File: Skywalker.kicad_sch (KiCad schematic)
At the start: 53 parts

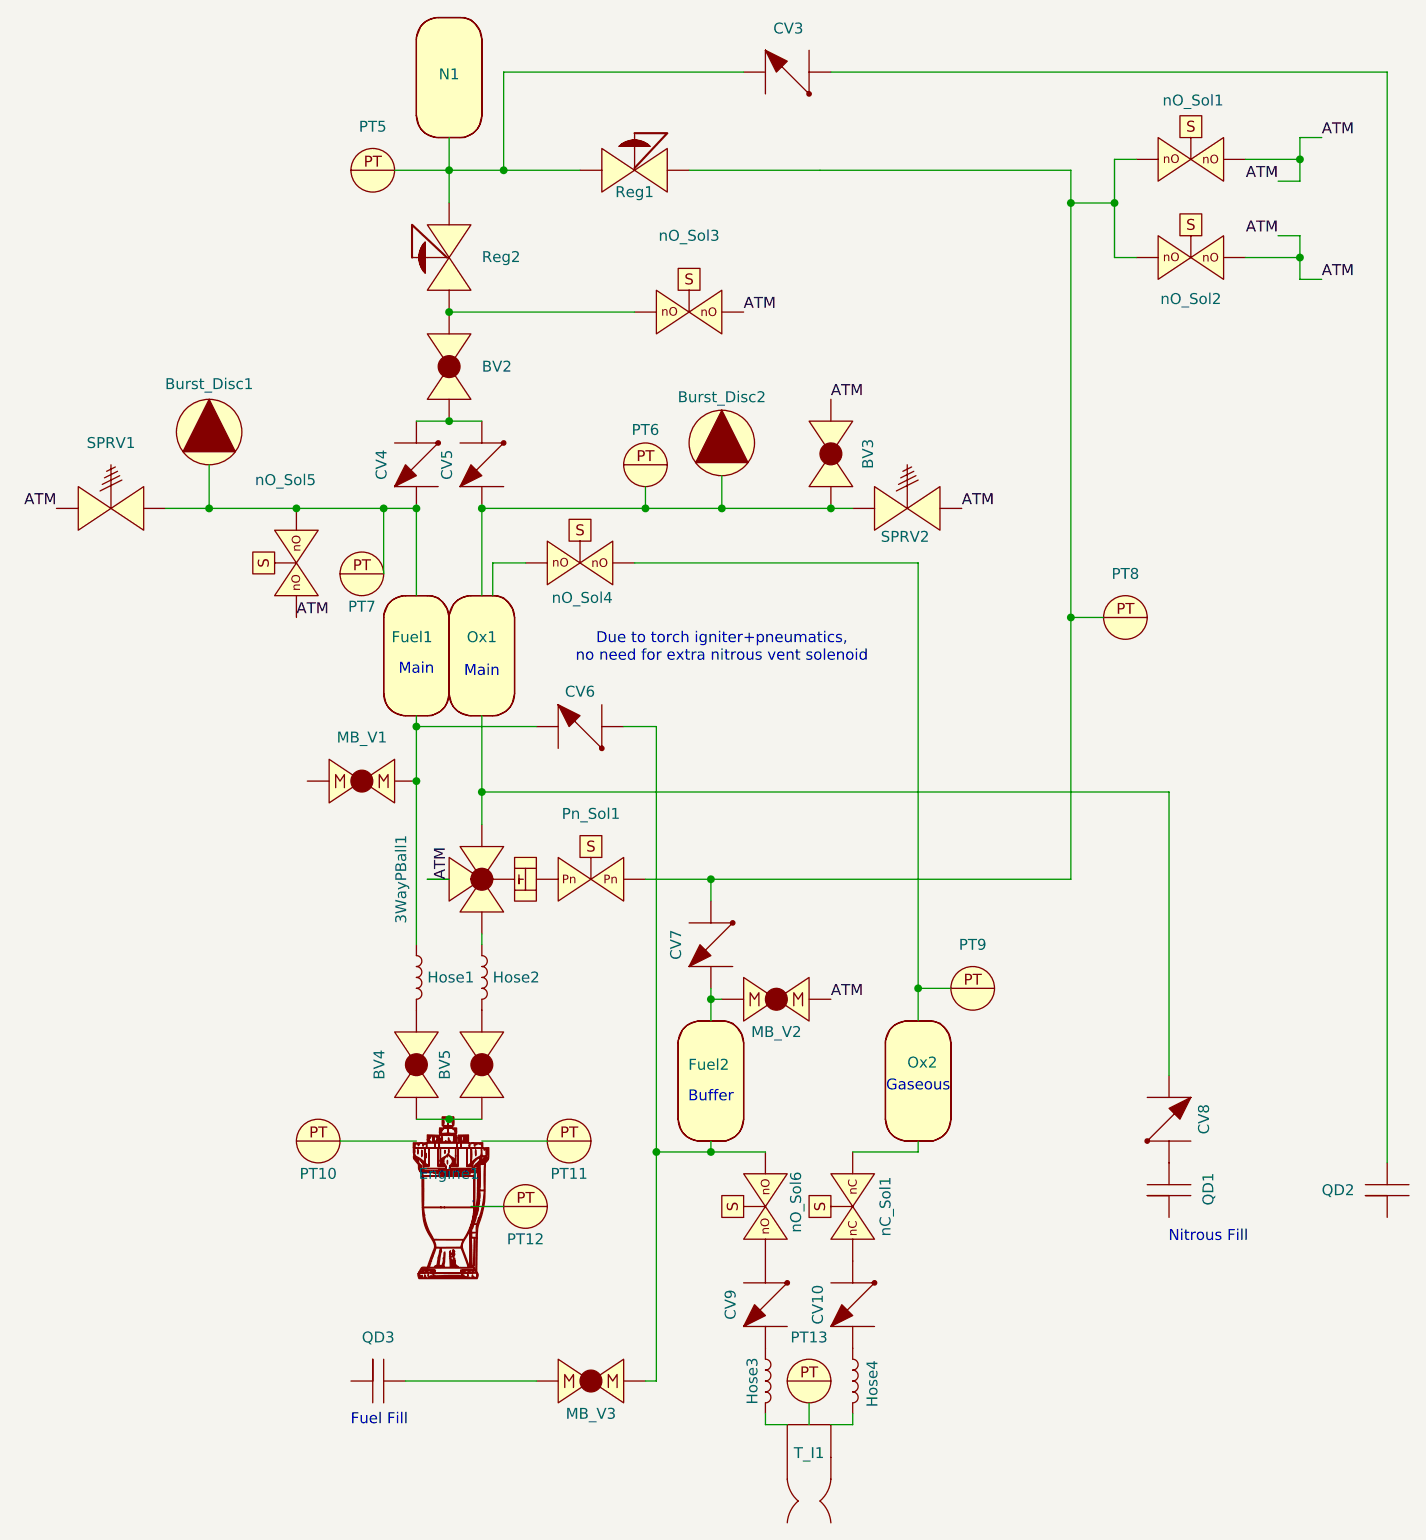
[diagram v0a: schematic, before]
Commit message: Updated igniter PID
+PT +nitrous pressure
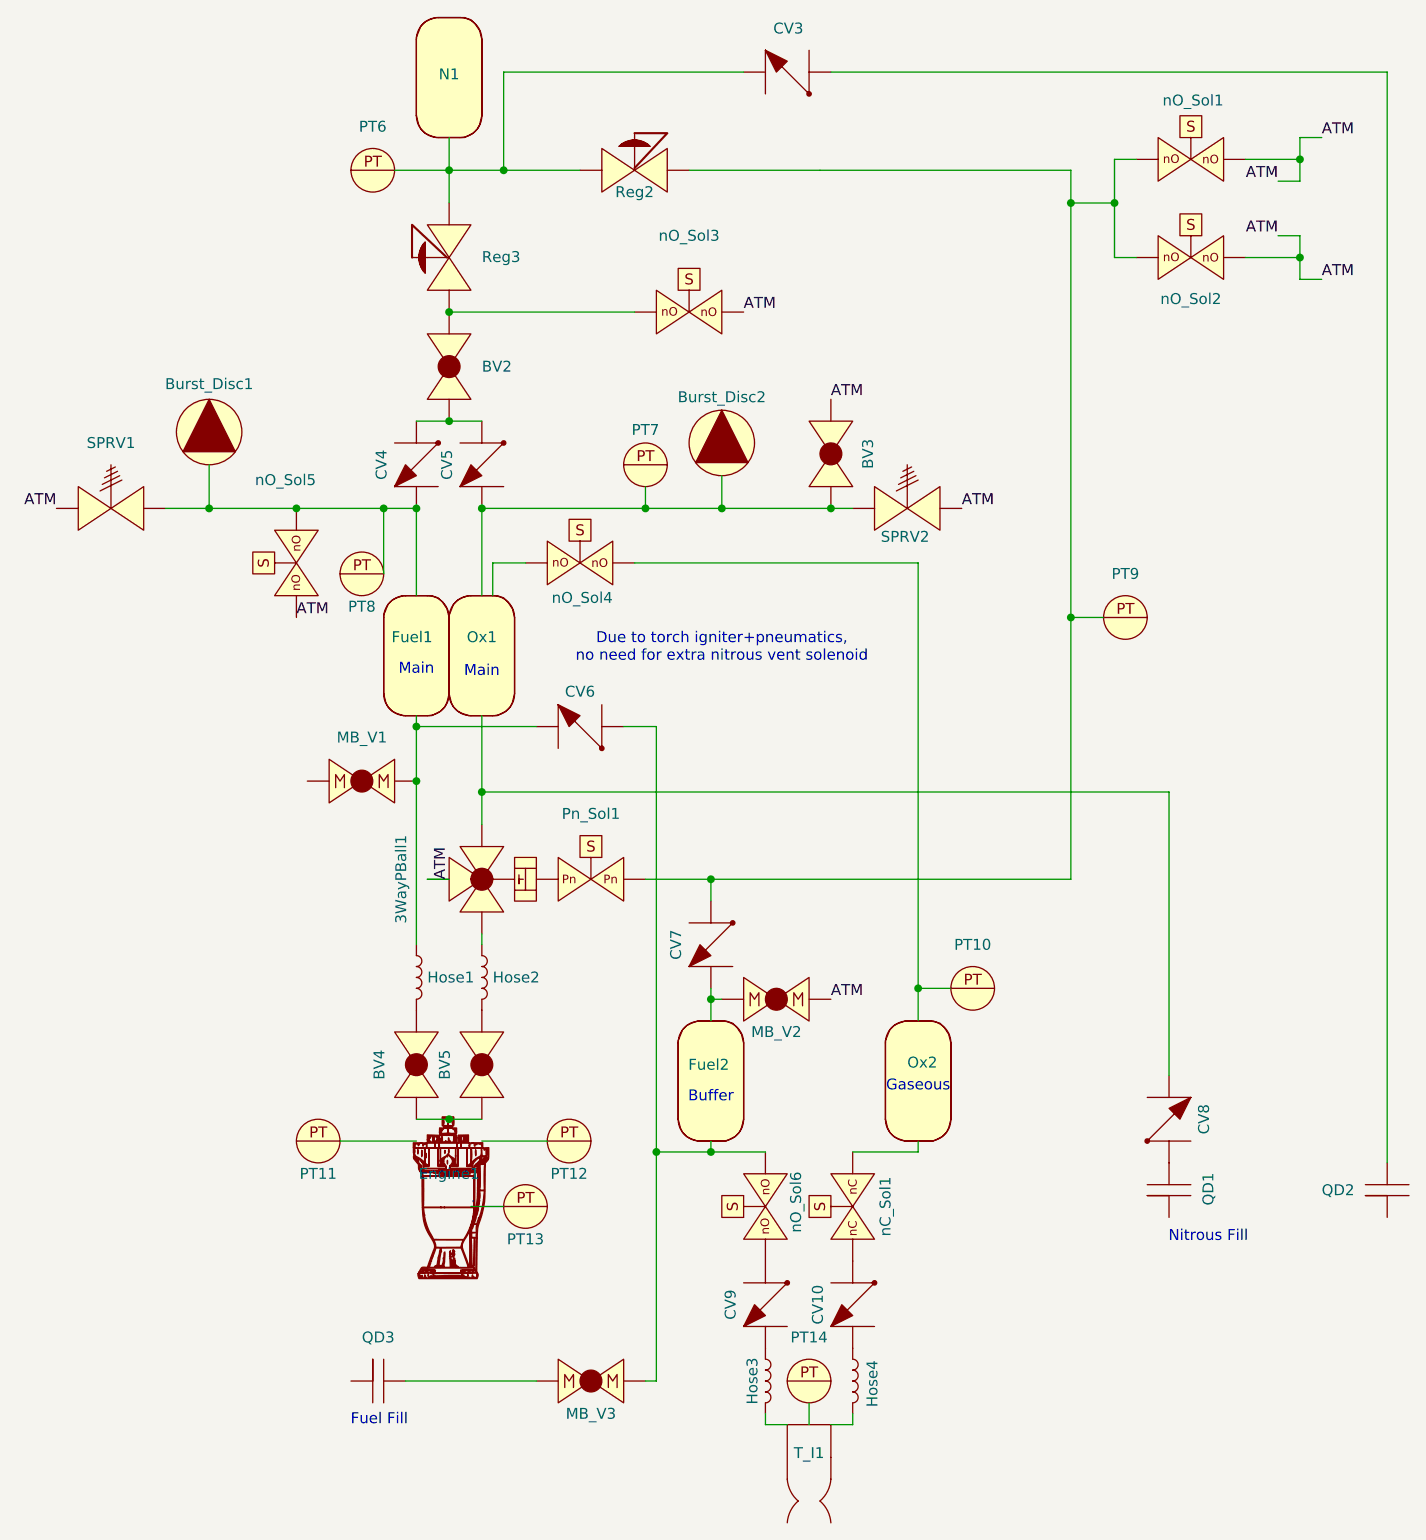
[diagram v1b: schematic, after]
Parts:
- renumbered PT9 to PT10, PT10 to PT11, PT11 to PT12, PT12 to PT13, PT13 to PT14, PT5 to PT6, PT6 to PT7, PT7 to PT8, PT8 to PT9, Reg1 to Reg2, Reg2 to Reg3
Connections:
- net at N1.: now also CV3., PT6., Reg2., Reg3.
- net at Engine1.: now also PT11.; no longer PT12.
- net at PT11.: no longer Engine1.
- net at CV10.: now also Hose4.1; no longer nC_Sol1.
- net at QD1.: now also CV8.
- new net: CV7., PT9., Pn_Sol1., Reg2., nO_Sol1., nO_Sol2.
- new net: CV7., Fuel2., MB_V2.
- new net: Engine1., PT12.
- new net: BV4., BV5., Engine1.
- new net: CV6., Fuel2., MB_V3., nO_Sol6.
- new net: CV10., nC_Sol1.
- new net: Burst_Disc1., CV4., Fuel1., PT8., SPRV1., nO_Sol5.
- new net: BV2., CV4., CV5.
- new net: Ox2., PT10., nO_Sol4.
- new net: 3WayPBall1., CV8., Ox1.
- new net: BV3., Burst_Disc2., CV5., Ox1., PT7., SPRV2.
- now unconnected: Burst_Disc1., Burst_Disc2., PT10., PT6., PT7., PT8., PT9.

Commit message: replaced servo with solenoid
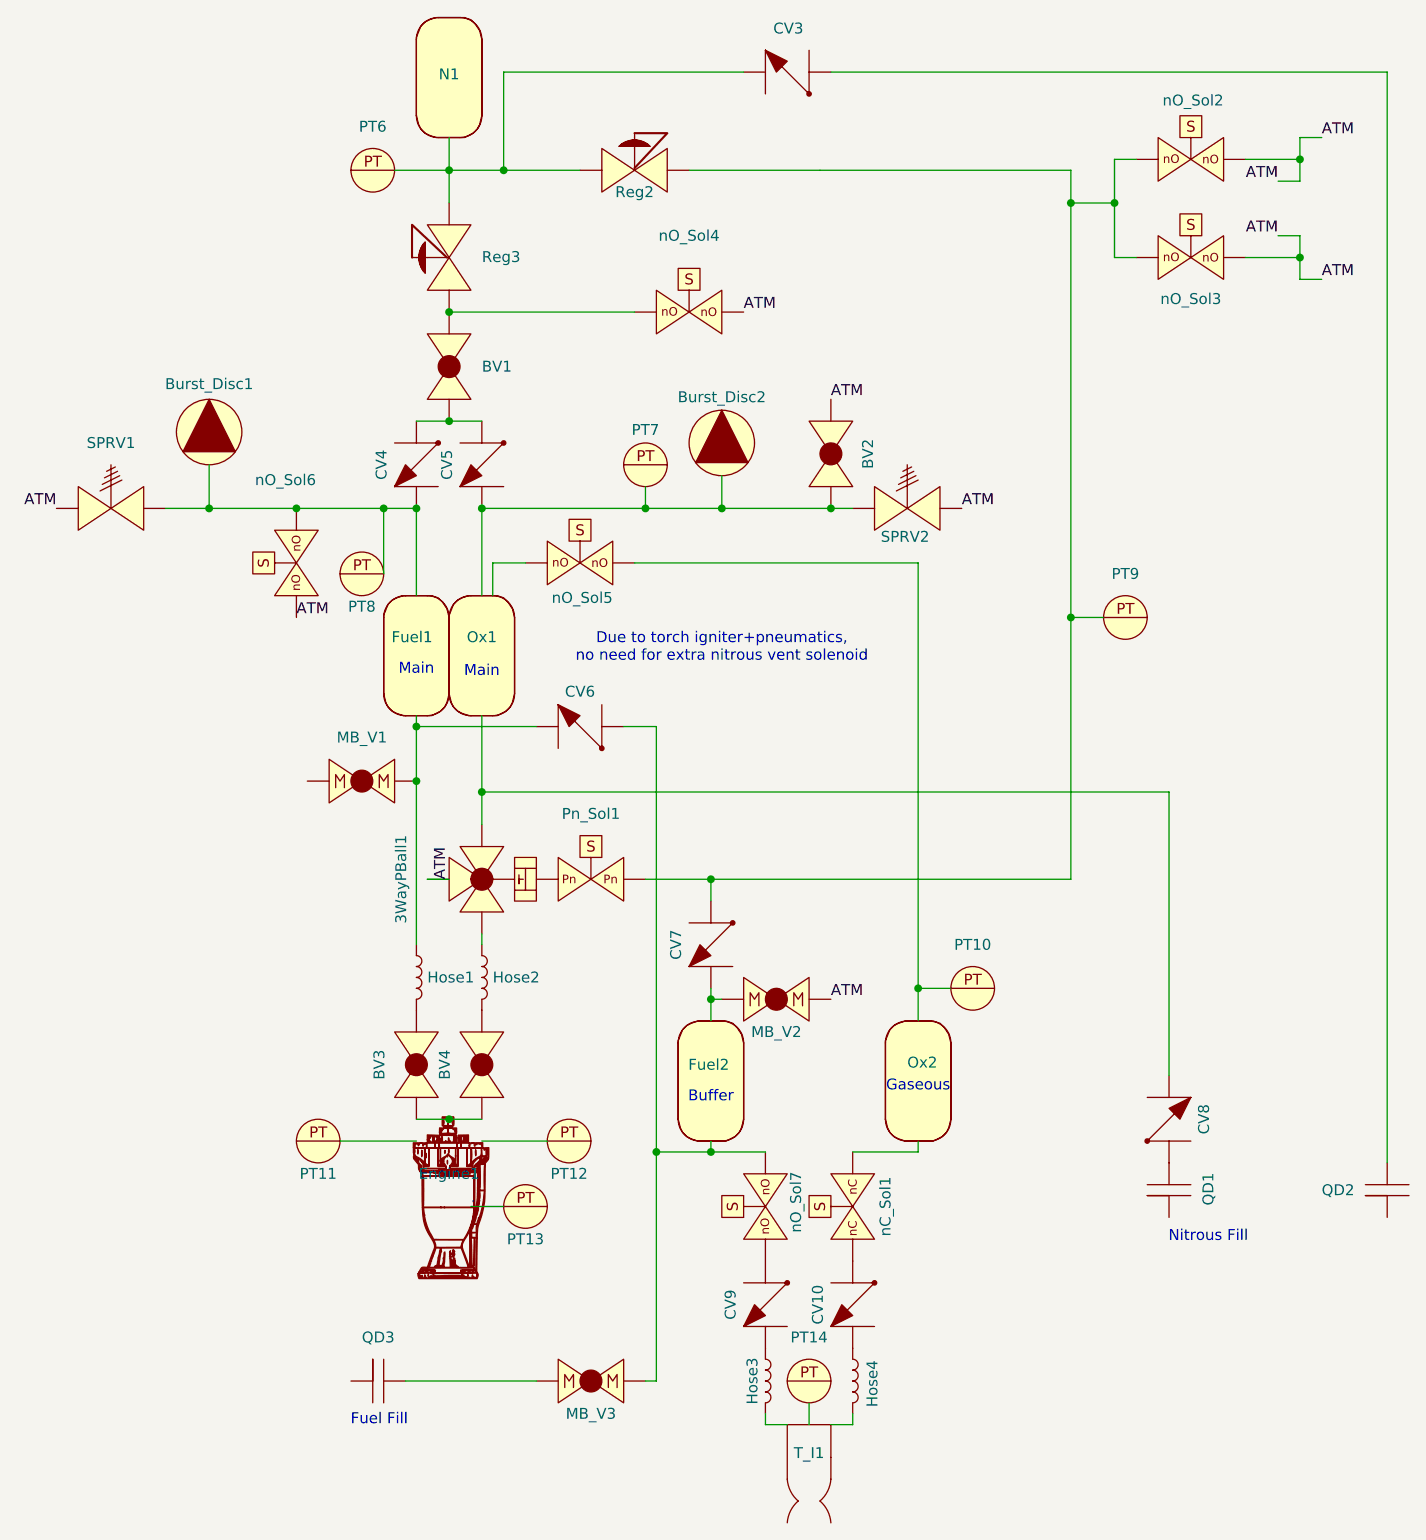
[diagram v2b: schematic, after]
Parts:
- renumbered BV2 to BV1, BV3 to BV2, BV4 to BV3, BV5 to BV4, nO_Sol1 to nO_Sol2, nO_Sol2 to nO_Sol3, nO_Sol3 to nO_Sol4, nO_Sol4 to nO_Sol5, nO_Sol5 to nO_Sol6, nO_Sol6 to nO_Sol7
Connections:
- net at N1.: now also CV3., PT6., Reg2., Reg3.
- net at Engine1.: now also PT11.; no longer PT12.
- net at PT11.: no longer Engine1.
- net at CV10.: now also Hose4.1; no longer nC_Sol1.
- net at QD1.: now also CV8.
- new net: CV7., PT9., Pn_Sol1., Reg2., nO_Sol2., nO_Sol3.
- new net: CV7., Fuel2., MB_V2.
- new net: Engine1., PT12.
- new net: BV3., BV4., Engine1.
- new net: CV6., Fuel2., MB_V3., nO_Sol7.
- new net: CV10., nC_Sol1.
- new net: Burst_Disc1., CV4., Fuel1., PT8., SPRV1., nO_Sol6.
- new net: BV1., CV4., CV5.
- new net: Ox2., PT10., nO_Sol5.
- new net: 3WayPBall1., CV8., Ox1.
- new net: BV2., Burst_Disc2., CV5., Ox1., PT7., SPRV2.
- now unconnected: Burst_Disc1., Burst_Disc2., PT10., PT6., PT7., PT8., PT9.
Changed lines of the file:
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@@
 		(on_board yes)
 		(dnp no)
-		(property "Reference" "BV5"
+		(property "Reference" "BV4"
 			(at 62.992 138.43 0)
 			(effects
@@
 			(project "P_IDs"
 				(path "/045f1f05-3134-4b6d-91b6-463031104f1e/8ff5724e-b29b-49c2-a1fa-190081404476"
-					(reference "BV5")
+					(reference "BV4")
 					(unit 1)
 				)
@@
 		(on_board yes)
 		(dnp no)
-		(property "Reference" "nO_Sol1"
+		(property "Reference" "nO_Sol2"
 			(at 150.114 26.162 0)
 			(effects
@@
 			(project "P_IDs"
 				(path "/045f1f05-3134-4b6d-91b6-463031104f1e/8ff5724e-b29b-49c2-a1fa-190081404476"
-					(reference "nO_Sol1")
+					(reference "nO_Sol2")
 					(unit 1)
 				)
@@
 		(on_board yes)
 		(dnp no)
-		(property "Reference" "BV3"
+		(property "Reference" "BV2"
 			(at 112.268 67.31 0)
 			(effects
@@
 			(project "P_IDs"
 				(path "/045f1f05-3134-4b6d-91b6-463031104f1e/8ff5724e-b29b-49c2-a1fa-190081404476"
-					(reference "BV3")
+					(reference "BV2")
 					(unit 1)
 				)
@@
 		(on_board yes)
 		(dnp no)
-		(property "Reference" "nO_Sol4"
+		(property "Reference" "nO_Sol5"
 			(at 78.994 84.074 0)
 			(effects
@@
 			(project "P_IDs"
 				(path "/045f1f05-3134-4b6d-91b6-463031104f1e/8ff5724e-b29b-49c2-a1fa-190081404476"
-					(reference "nO_Sol4")
+					(reference "nO_Sol5")
 					(unit 1)
 				)
@@
 		(dnp no)
 		(fields_autoplaced yes)
-		(property "Reference" "BV2"
+		(property "Reference" "BV1"
 			(at 67.31 57.1499 90)
 			(effects
@@
 			(project ""
 				(path "/045f1f05-3134-4b6d-91b6-463031104f1e/8ff5724e-b29b-49c2-a1fa-190081404476"
-					(reference "BV2")
+					(reference "BV1")
 					(unit 1)
 				)
@@
 		(dnp no)
 		(fields_autoplaced yes)
-		(property "Reference" "nO_Sol3"
+		(property "Reference" "nO_Sol4"
 			(at 91.44 41.91 0)
 			(effects
@@
 			(project "P_IDs"
 				(path "/045f1f05-3134-4b6d-91b6-463031104f1e/8ff5724e-b29b-49c2-a1fa-190081404476"
-					(reference "nO_Sol3")
+					(reference "nO_Sol4")
 					(unit 1)
 				)
@@
 		(on_board yes)
 		(dnp no)
-		(property "Reference" "BV4"
+		(property "Reference" "BV3"
 			(at 55.372 138.43 0)
 			(effects
@@
 			(project "P_IDs"
 				(path "/045f1f05-3134-4b6d-91b6-463031104f1e/8ff5724e-b29b-49c2-a1fa-190081404476"
-					(reference "BV4")
+					(reference "BV3")
 					(unit 1)
 				)
@@
 		(on_board yes)
 		(dnp no)
-		(property "Reference" "nO_Sol6"
+		(property "Reference" "nO_Sol7"
 			(at 103.886 150.876 0)
 			(effects
@@
 			(project "P_IDs"
 				(path "/045f1f05-3134-4b6d-91b6-463031104f1e/8ff5724e-b29b-49c2-a1fa-190081404476"
-					(reference "nO_Sol6")
+					(reference "nO_Sol7")
 					(unit 1)
 				)
@@
 		(on_board yes)
 		(dnp no)
-		(property "Reference" "nO_Sol2"
+		(property "Reference" "nO_Sol3"
 			(at 149.86 49.276 0)
 			(effects
@@
 			(project "P_IDs"
 				(path "/045f1f05-3134-4b6d-91b6-463031104f1e/8ff5724e-b29b-49c2-a1fa-190081404476"
-					(reference "nO_Sol2")
+					(reference "nO_Sol3")
 					(unit 1)
 				)
@@
 		(on_board yes)
 		(dnp no)
-		(property "Reference" "nO_Sol5"
+		(property "Reference" "nO_Sol6"
 			(at 40.894 70.358 90)
 			(effects
@@
 			(project "P_IDs"
 				(path "/045f1f05-3134-4b6d-91b6-463031104f1e/8ff5724e-b29b-49c2-a1fa-190081404476"
-					(reference "nO_Sol5")
-					(unit 1)
-				)
+					(reference "nO_Sol6")
+					(unit 1)
+				)

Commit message: rebase
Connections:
- net at N1.: now also CV3., PT6., Reg2., Reg3.
- net at Engine1.: now also PT11.; no longer PT12.
- net at PT11.: no longer Engine1.
- net at CV10.: now also Hose4.1; no longer nC_Sol1.
- net at QD1.: now also CV8.
- new net: CV7., PT9., Pn_Sol1., Reg2., nO_Sol2., nO_Sol3.
- new net: CV7., Fuel2., MB_V2.
- new net: Engine1., PT12.
- new net: BV3., BV4., Engine1.
- new net: CV6., Fuel2., MB_V3., nO_Sol7.
- new net: CV10., nC_Sol1.
- new net: Burst_Disc1., CV4., Fuel1., PT8., SPRV1., nO_Sol6.
- new net: BV1., CV4., CV5.
- new net: Ox2., PT10., nO_Sol5.
- new net: 3WayPBall1., CV8., Ox1.
- new net: BV2., Burst_Disc2., CV5., Ox1., PT7., SPRV2.
- now unconnected: Burst_Disc1., Burst_Disc2., PT10., PT6., PT7., PT8., PT9.
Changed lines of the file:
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@@
 	(label "ATM"
 		(at 17.78 73.66 180)
+		(fields_autoplaced yes)
 		(effects
 			(font
@@
 	(label "ATM"
 		(at 160.02 41.91 180)
+		(fields_autoplaced yes)
 		(effects
 			(font
@@
 	(label "ATM"
 		(at 165.1 46.99 0)
+		(fields_autoplaced yes)
 		(effects
 			(font
@@
 	(label "ATM"
 		(at 123.19 73.66 0)
+		(fields_autoplaced yes)
 		(effects
 			(font
@@
 	(label "."
 		(at 66.04 154.94 0)
+		(fields_autoplaced yes)
 		(effects
 			(font
@@
 	(label "ATM"
 		(at 107.95 130.81 0)
+		(fields_autoplaced yes)
 		(effects
 			(font
@@
 	(label "ATM"
 		(at 165.1 30.48 0)
+		(fields_autoplaced yes)
 		(effects
 			(font
@@
 	(label "."
 		(at 105.41 180.34 0)
+		(fields_autoplaced yes)
 		(effects
 			(font
@@
 	(label "."
 		(at 68.58 83.82 0)
+		(fields_autoplaced yes)
 		(effects
 			(font
@@
 	(label "ATM"
 		(at 97.79 50.8 0)
+		(fields_autoplaced yes)
 		(effects
 			(font
@@
 	(label "ATM"
 		(at 63.5 116.84 90)
+		(fields_autoplaced yes)
 		(effects
 			(font
@@
 	(label "ATM"
 		(at 45.72 86.36 0)
+		(fields_autoplaced yes)
 		(effects
 			(font
@@
 	(label "ATM"
 		(at 107.95 60.96 0)
+		(fields_autoplaced yes)
 		(effects
 			(font
@@
 	(label "ATM"
 		(at 160.02 35.56 180)
+		(fields_autoplaced yes)
 		(effects
 			(font
